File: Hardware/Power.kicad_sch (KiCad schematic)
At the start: 1 part, among them J1 2309413-1

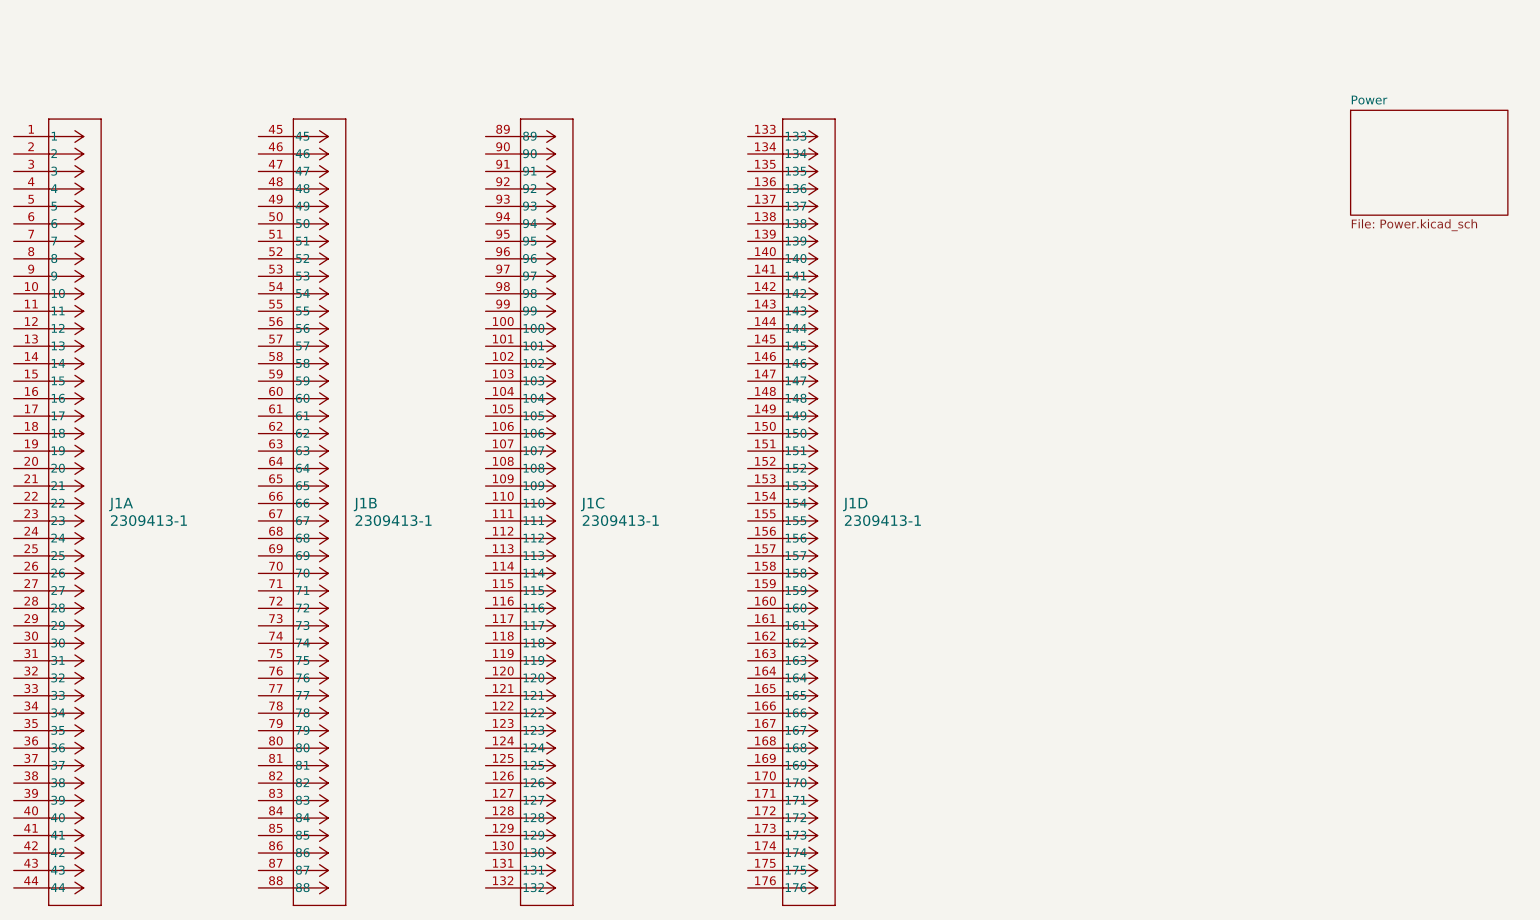
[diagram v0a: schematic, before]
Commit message: Added camera serializer and libraries
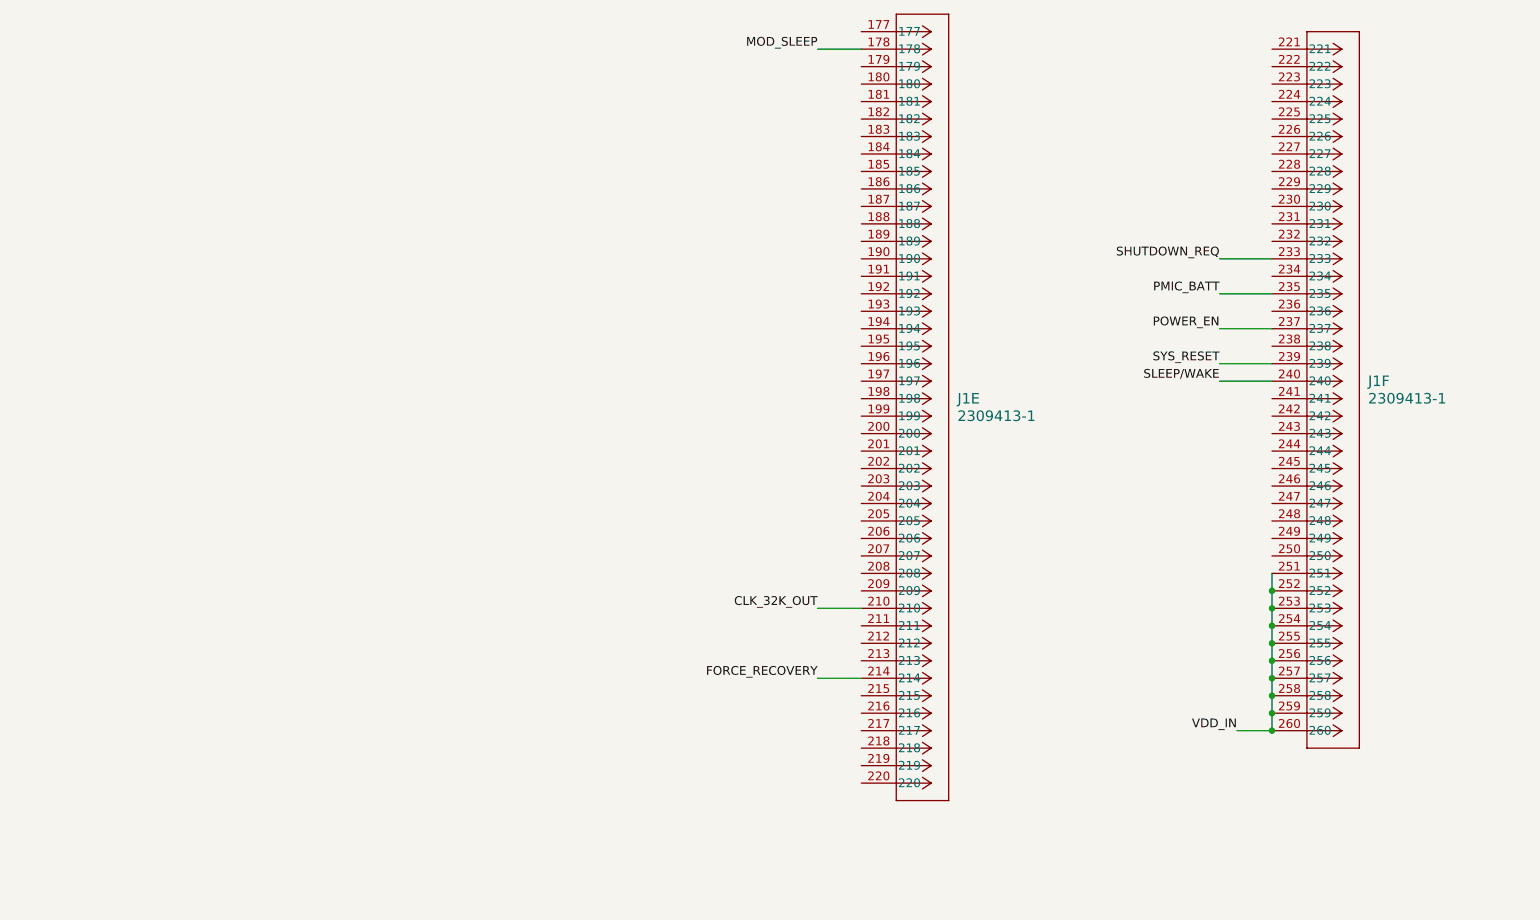
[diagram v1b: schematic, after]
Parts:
- removed J1: 2309413-1, 2309413-1:CONN260_2309413-1_TEC, symbol 2309413-1:2309413-1
- added J1: 2309413-1, 2309413-1:CONN260_2309413-1_TEC, symbol 2309413-1:2309413-1
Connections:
- new net CLK_32K_OUT: J1.210
- new net FORCE_RECOVERY: J1.214
- new net MOD_SLEEP: J1.178
- new net PMIC_BATT: J1.235
- new net POWER_EN: J1.237
- new net SHUTDOWN_REQ: J1.233
- new net SLEEP/WAKE: J1.240
- new net SYS_RESET: J1.239
- new net VDD_IN: J1.251, J1.252, J1.253, J1.254, J1.255, J1.256, J1.257, J1.258, J1.259, J1.260
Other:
- removed sheet Power
